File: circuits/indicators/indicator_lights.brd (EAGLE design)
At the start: 8.9 x 18.2 mm, 6 parts, among them Q1 BSS84

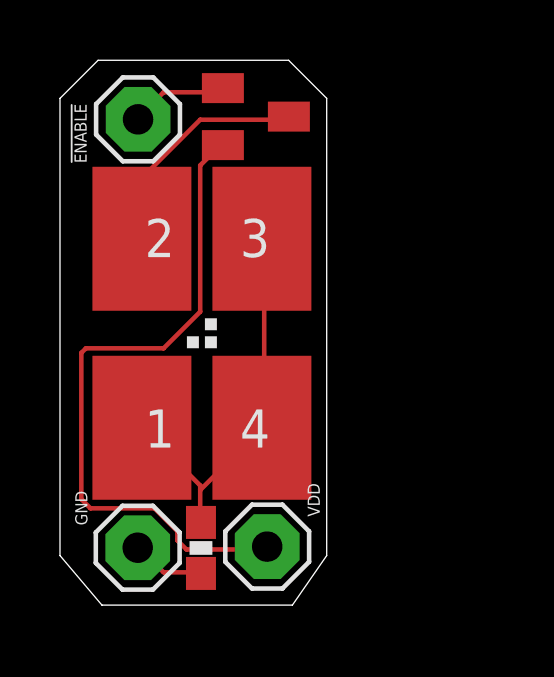
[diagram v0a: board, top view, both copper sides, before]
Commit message: Added new LED layout
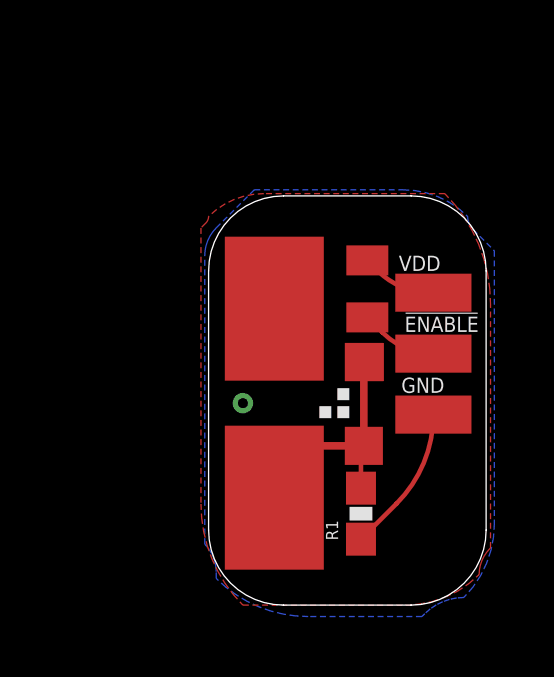
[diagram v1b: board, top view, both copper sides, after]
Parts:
- removed LSP1, LSP2, LSP3: MCS10B, solpad:MCS10B
- added !ENABLE, GND, VDD: (no value), wirepad:SMD1,27-2,54
- moved Q1 6.31 mm to (10.4, 11.4), turned to 90 degrees
- moved R1 5.46 mm to (11.3, 3.94)
- moved LED1 4.99 mm to (10.4, 7.62)
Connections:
- net !ENABLE: now also !ENABLE.1; no longer LSP1.MP
- net GND: now also GND.1; no longer LSP3.MP
- net VDD: now also VDD.1; no longer LSP2.MP
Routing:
- net VDD: track 22.4 -> 2.49 mm
- net N$1: track 7.85 -> 1.14 mm
- net N$2: track 13.3 -> 8.53 mm
- net GND: track 2.46 -> 4.89 mm
- net !ENABLE: track 3.28 -> 2.55 mm
- added copper zone on layer 1, net GND
- added copper zone on layer 16, net N$2
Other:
- board size 8.9 x 18.2 mm -> 9.3 x 13.6 mm
- board text removed: "!ENABLE"
- board text removed: "GND"
- board text removed: "VDD"
